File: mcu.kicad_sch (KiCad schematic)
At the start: 54 parts, among them J69 Conn_01x22, J70 Conn_01x22, J71 Conn_01x22, J72 Conn_01x22, J73 Conn_01x22, J74 Conn_01x22, J75 Conn_01x22, J76 Conn_01x22, J77 Conn_01x22, J78 Conn_01x22

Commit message: WIP v0.2.0 changes
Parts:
- removed J69, J70, J71, J72, J73, J74, J75, J76, J77, J78: Conn_01x22, HL_Connector_Pad_2.54mm:Pad_1x22_P2.54_1.7x1.7_Oct, symbol Connector_Generic:Conn_01x22
- removed R120, R121, R147, R148, R149, R150, R151, R152, R153, R154, R155, R156, R157, R158, R159: 1k, Resistor_SMD:R_0402_1005Metric, symbol Device:R_Small
- added J63, J64, J65, J66, J92, J93, J94, J95: Conn_01x20, HL_Connector_Pad_2.54mm:Pad_1x20_P2.54_1.7x1.7_Oct, symbol Connector_Generic:Conn_01x20
- added J96, J97: Conn_01x03, HL_Connector_Pad_2.54mm:Pad_1x03_P2.54_1.7x1.7_Rnd-Rect-Rnd, symbol Connector_Generic:Conn_01x03
- added U36: RPi_Pico_SMD_TH, HL_Module:RPi_Pico_Outline, symbol HL_MCU_Module:RPi_Pico_SMD_TH
- R129, R130: value 1k -> 3.3k; footprint Resistor_SMD:R_0402_1005Metric -> Resistor_SMD:R_0603_1608Metric; LCSC C11702 -> C22978
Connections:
- net at R126.1: now also J63.7 (Pin_7)
- net at R126.2: now also J64.7 (Pin_7), J92.7 (Pin_7), J93.7 (Pin_7), U36.34 (GPIO28_ADC2)
- net at R146.1: now also J66.1 (Pin_1)
- net at R146.2: now also J65.1 (Pin_1), J94.1 (Pin_1), J95.1 (Pin_1), U36.1 (GPIO0)
- net at R138.1: now also J66.11 (Pin_11)
- net at R139.1: now also J66.10 (Pin_10)
- net at R140.1: now also J66.9 (Pin_9)
- net at R141.1: now also J66.7 (Pin_7)
- net at R142.1: now also J66.6 (Pin_6)
- net at R143.1: now also J66.5 (Pin_5)
- net at R144.1: now also J66.4 (Pin_4)
- net at R145.1: now also J66.2 (Pin_2)
- net at R116.2: now also J64.20 (Pin_20), J92.20 (Pin_20), J93.20 (Pin_20), U36.21 (GPIO16)
- net at R125.2: now also J64.9 (Pin_9), J92.9 (Pin_9), J93.9 (Pin_9), U36.32 (GPIO27_ADC1)
- net at R127.2: now also J64.6 (Pin_6), J92.6 (Pin_6), J93.6 (Pin_6), U36.35 (ADC_VREF)
- net +3.3V: now reaches R128.2
- net +3.3V: now also R129.1, R130.1, J64.5 (Pin_5), J92.5 (Pin_5), J93.5 (Pin_5), U36.36 (3V3)
- net SCL: now reaches R129.2
- net SCL: now also J63.14 (Pin_14), J64.14 (Pin_14), J92.14 (Pin_14), J93.14 (Pin_14), U36.27 (GPIO21)
- net SDA: now reaches R130.2
- net SDA: now also J63.15 (Pin_15), J64.15 (Pin_15), J92.15 (Pin_15), J93.15 (Pin_15), U36.26 (GPIO20)
- net at R131.2: now also J65.20 (Pin_20), J94.20 (Pin_20), J95.20 (Pin_20), U36.20 (GPIO15)
- net at R132.2: now also J65.19 (Pin_19), J94.19 (Pin_19), J95.19 (Pin_19), U36.19 (GPIO14)
- net at R133.2: now also J65.17 (Pin_17), J94.17 (Pin_17), J95.17 (Pin_17), U36.17 (GPIO13)
- net at R134.2: now also J65.16 (Pin_16), J94.16 (Pin_16), J95.16 (Pin_16), U36.16 (GPIO12)
- net at R117.2: now also J64.19 (Pin_19), J92.19 (Pin_19), J93.19 (Pin_19), U36.22 (GPIO17)
- net at R135.2: now also J65.15 (Pin_15), J94.15 (Pin_15), J95.15 (Pin_15), U36.15 (GPIO11)
- net at R136.2: now also J65.14 (Pin_14), J94.14 (Pin_14), J95.14 (Pin_14), U36.14 (GPIO10)
- net at R137.2: now also J65.12 (Pin_12), J94.12 (Pin_12), J95.12 (Pin_12), U36.12 (GPIO9)
- net at R118.2: now also J64.17 (Pin_17), J92.17 (Pin_17), J93.17 (Pin_17), U36.24 (GPIO18)
- net at R119.2: now also J64.16 (Pin_16), J92.16 (Pin_16), J93.16 (Pin_16), U36.25 (GPIO19)
- net at R122.2: now also J64.12 (Pin_12), J92.12 (Pin_12), J93.12 (Pin_12), U36.29 (GPIO22)
- net at R123.2: now also J64.11 (Pin_11), J92.11 (Pin_11), J93.11 (Pin_11), U36.30 (RUN)
- net at R124.2: now also J64.10 (Pin_10), J92.10 (Pin_10), J93.10 (Pin_10), U36.31 (GPIO26_ADC0)
- net at R138.2: now also J65.11 (Pin_11), J94.11 (Pin_11), J95.11 (Pin_11), U36.11 (GPIO8)
- net at R139.2: now also J65.10 (Pin_10), J94.10 (Pin_10), J95.10 (Pin_10), U36.10 (GPIO7)
- net at R140.2: now also J65.9 (Pin_9), J94.9 (Pin_9), J95.9 (Pin_9), U36.9 (GPIO6)
- net at R141.2: now also J65.7 (Pin_7), J94.7 (Pin_7), J95.7 (Pin_7), U36.7 (GPIO5)
- net at R142.2: now also J65.6 (Pin_6), J94.6 (Pin_6), J95.6 (Pin_6), U36.6 (GPIO4)
- net at R143.2: now also J65.5 (Pin_5), J94.5 (Pin_5), J95.5 (Pin_5), U36.5 (GPIO3)
- net at R144.2: now also J65.4 (Pin_4), J94.4 (Pin_4), J95.4 (Pin_4), U36.4 (GPIO2)
- net at R145.2: now also J65.2 (Pin_2), J94.2 (Pin_2), J95.2 (Pin_2), U36.2 (GPIO1)
- net at R133.1: now also J66.17 (Pin_17)
- net at R137.1: now also J66.12 (Pin_12)
- net at R134.1: now also J66.16 (Pin_16)
- net at R116.1: now also J63.20 (Pin_20)
- net at R135.1: now also J66.15 (Pin_15)
- net at R128.1: now also J63.5 (Pin_5)
- net at R125.1: now also J63.9 (Pin_9)
- net at R127.1: now also J63.6 (Pin_6)
- net at R131.1: now also J66.20 (Pin_20)
- net at R132.1: now also J66.19 (Pin_19)
- net at R117.1: now also J63.19 (Pin_19)
- net at R136.1: now also J66.14 (Pin_14)
- net at R118.1: now also J63.17 (Pin_17)
- net at R119.1: now also J63.16 (Pin_16)
- net at R122.1: now also J63.12 (Pin_12)
- net at R123.1: now also J63.11 (Pin_11)
- net at R124.1: now also J63.10 (Pin_10)
- new net: J63.2 (Pin_2), J64.2 (Pin_2), J92.2 (Pin_2), J93.2 (Pin_2), U36.39 (VSYS)
- new net: J63.4 (Pin_4), J64.4 (Pin_4), J92.4 (Pin_4), J93.4 (Pin_4), U36.37 (3V3_EN)
- new net: J63.8 (Pin_8), J64.8 (Pin_8), J92.8 (Pin_8), J93.8 (Pin_8), U36.33 (AGND)
- new net: J96.1 (Pin_1), J97.1 (Pin_1), U36.43 (SWDIO)
- new net: J96.3 (Pin_3), J97.3 (Pin_3), U36.41 (SWCLK)
- new net +5V: J63.1 (Pin_1), J64.1 (Pin_1), J92.1 (Pin_1), J93.1 (Pin_1), U36.40 (VBUS)
- new net GND: J63.13 (Pin_13), J63.18 (Pin_18), J63.3 (Pin_3), J64.13 (Pin_13), J64.18 (Pin_18), J64.3 (Pin_3), J65.13 (Pin_13), J65.18 (Pin_18), J65.3 (Pin_3), J65.8 (Pin_8), J66.13 (Pin_13), J66.18 (Pin_18), J66.3 (Pin_3), J66.8 (Pin_8), J92.13 (Pin_13), J92.18 (Pin_18), J92.3 (Pin_3), J93.13 (Pin_13), J93.18 (Pin_18), J93.3 (Pin_3), J94.13 (Pin_13), J94.18 (Pin_18), J94.3 (Pin_3), J94.8 (Pin_8), J95.13 (Pin_13), J95.18 (Pin_18), J95.3 (Pin_3), J95.8 (Pin_8), J96.2 (Pin_2), J97.2 (Pin_2), U36.13 (GND), U36.18 (GND), U36.23 (GND), U36.28 (GND), U36.3 (GND), U36.38 (GND), U36.42 (GND), U36.8 (GND)

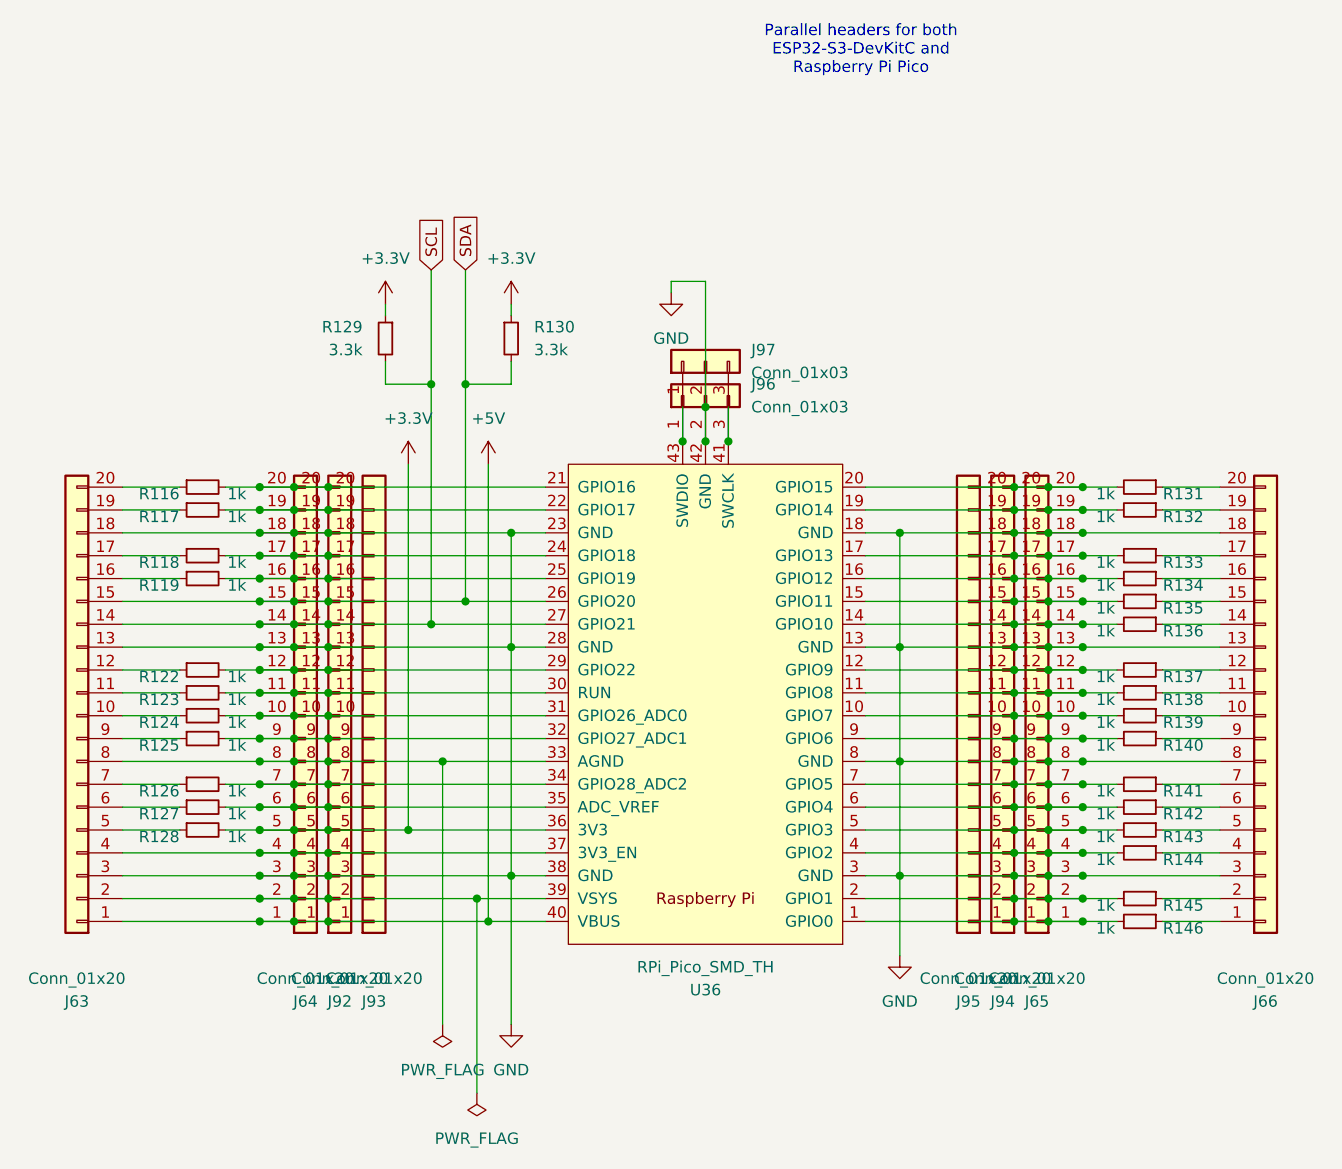
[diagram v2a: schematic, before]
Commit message: Assign part numbers and finish other 0.2.0 changes
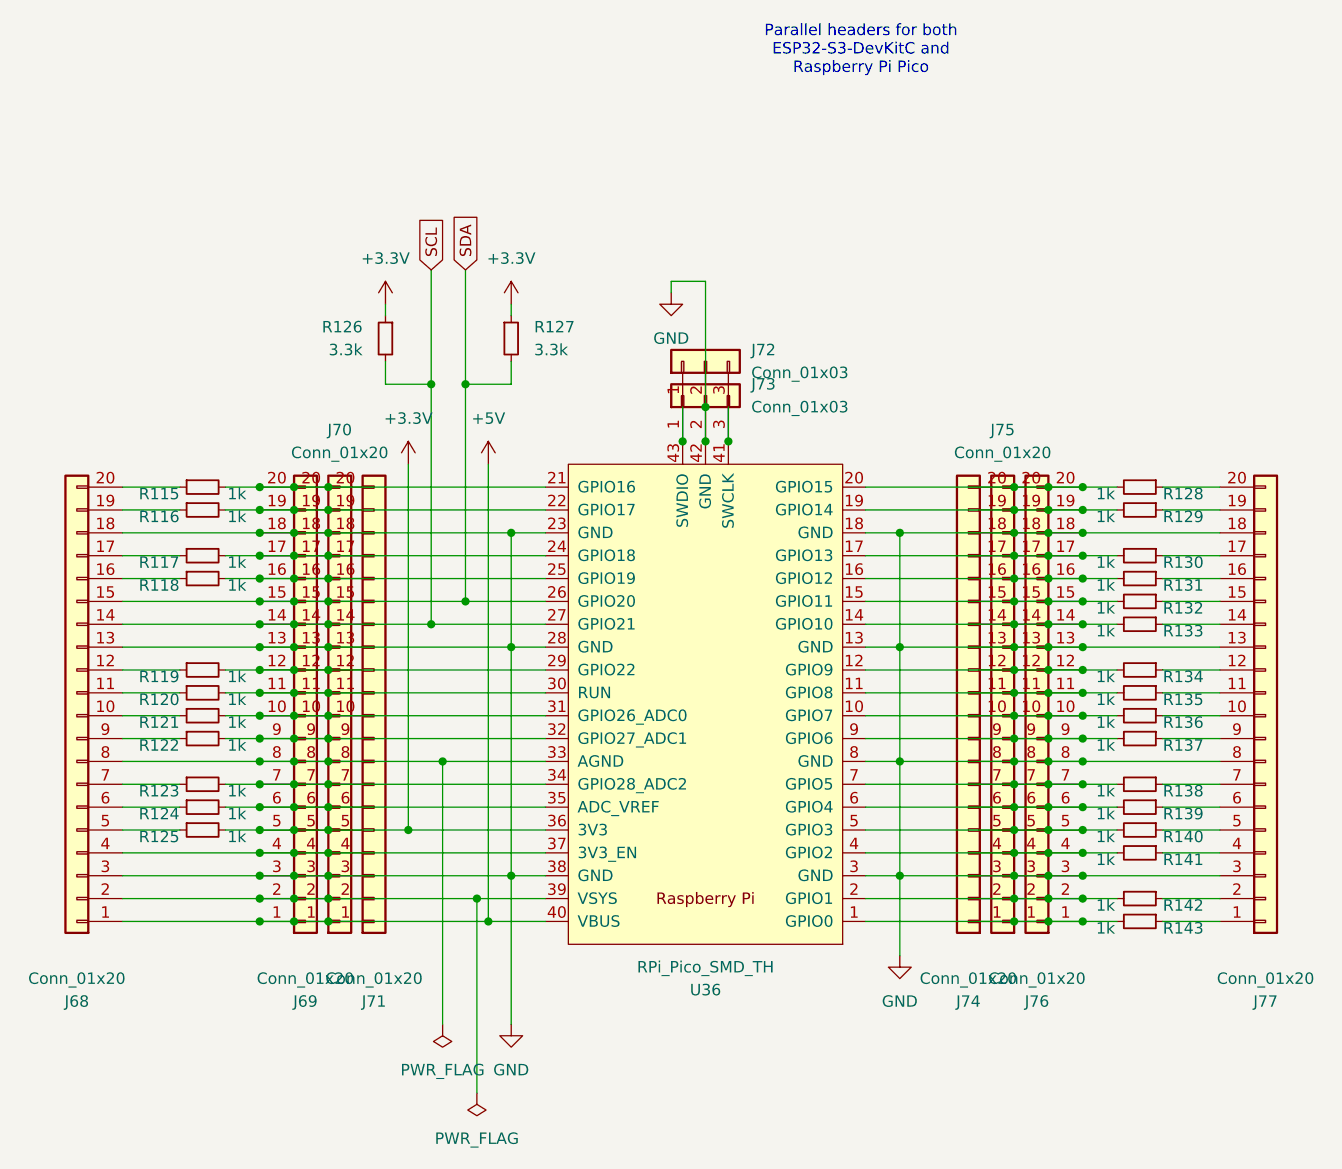
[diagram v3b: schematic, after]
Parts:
- J68: renamed from J63; LCSC (none) -> C50981
- J69: renamed from J64; LCSC§ (none) -> C50981
- J70: renamed from J92; LCSC (none) -> C2905423
- J75: renamed from J94; LCSC (none) -> C2905423
- J76: renamed from J65; LCSC (none) -> C50981
- J77: renamed from J66; LCSC (none) -> C50981
- renumbered J93 to J71, J97 to J72, J96 to J73, J95 to J74, R116 to R115, R117 to R116, R118 to R117, R119 to R118, R122 to R119, R123 to R120, R124 to R121, R125 to R122, R126 to R123, R127 to R124, R128 to R125, R129 to R126, R130 to R127, R131 to R128, R132 to R129, R133 to R130, R134 to R131, R135 to R132, R136 to R133, R137 to R134, R138 to R135, R139 to R136, R140 to R137, R141 to R138, R142 to R139, R143 to R140, R144 to R141, R145 to R142, R146 to R143

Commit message: Update the title blocks
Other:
- company: (none) -> Hat Labs Oy
- title: (none) -> HALSPA - Hat Labs Spaghetti Board
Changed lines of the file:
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@@
 	(generator_version "9.0")
 	(paper "A4")
+	(title_block
+		(title "HALSPA - Hat Labs Spaghetti Board")
+		(date "2025-04-17")
+		(rev "v0.2.0")
+		(company "Hat Labs Oy")
+		(comment 1 "See the accompanying LICENSE.md file for license details.")
+	)
 	(text "Parallel headers for both\nESP32-S3-DevKitC and\nRaspberry Pi Pico"
 		(exclude_from_sim no)

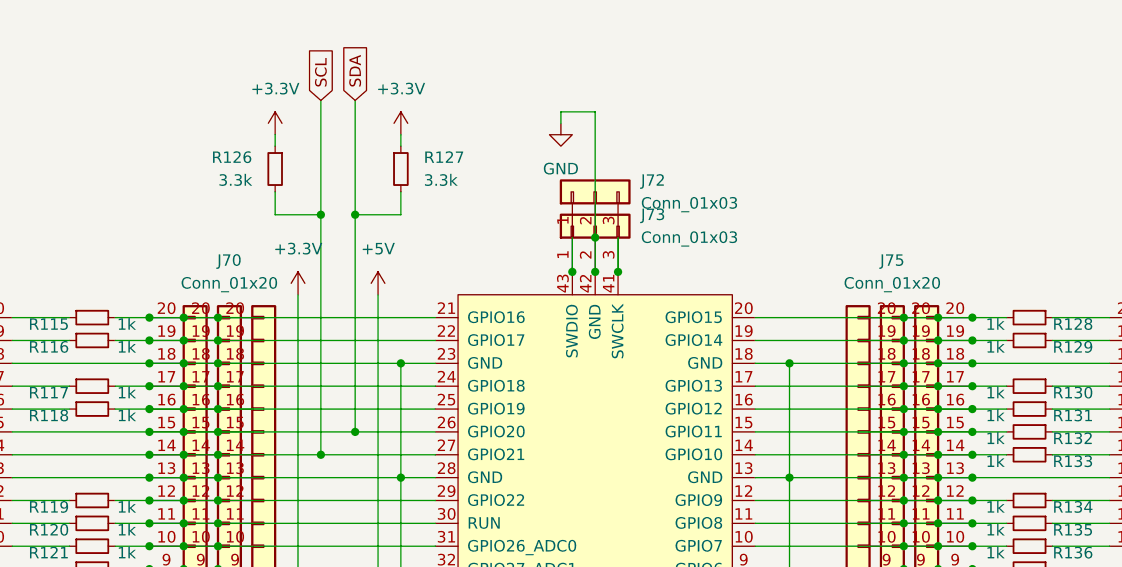
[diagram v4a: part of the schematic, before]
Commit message: Add JLCPCB corrections
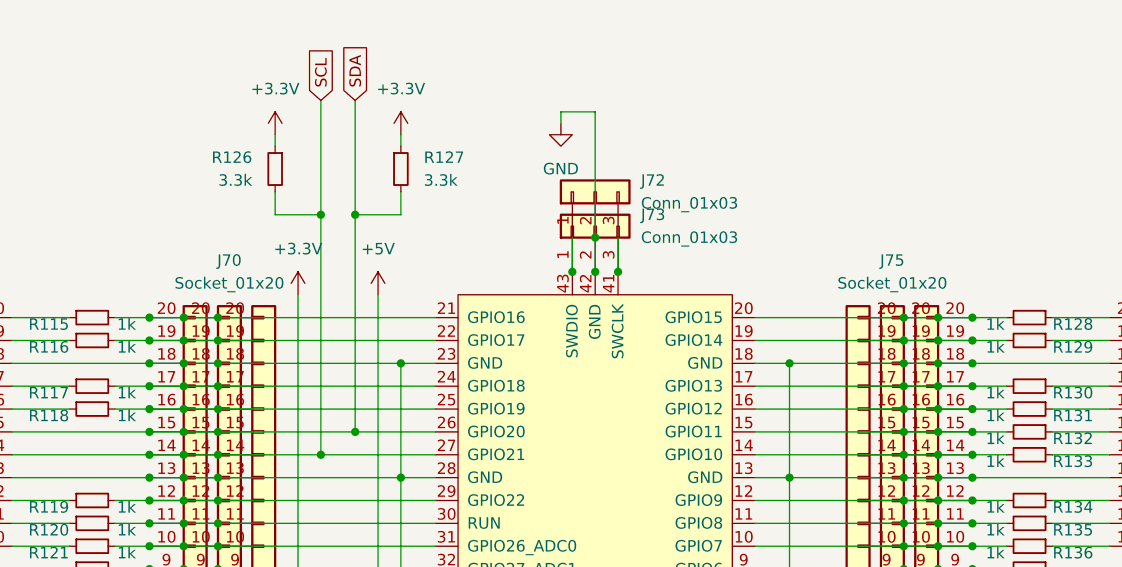
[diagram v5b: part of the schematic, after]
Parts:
- J68, J76, J77: JLCPCB_CORRECTION (none) -> 0;24.13;270
- J69: JLCPCB_CORRECTION (none) -> 0;24.13;270; LCSC (none) -> C50981; LCSC§ C50981 -> (none)
- J70, J75: value Conn_01x20 -> Socket_01x20; JLCPCB_CORRECTION (none) -> 0;24.13;270
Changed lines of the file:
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@@
+			)
+		)
+		(property "JLCPCB_CORRECTION" "0;24.13;270"
+			(at 171.45 96.52 0)
+			(effects
+				(font
+					(size 1.27 1.27)
+				)
+				(hide yes)
 			)
 		)
@@
 			)
 		)
-		(property "Value" "Conn_01x20"
+		(property "Value" "Socket_01x20"
 			(at 93.98 67.31 0)
 			(effects
@@
 		)
 		(property "LCSC" "C2905423"
+			(at 93.98 96.52 0)
+			(effects
+				(font
+					(size 1.27 1.27)
+				)
+				(hide yes)
+			)
+		)
+		(property "JLCPCB_CORRECTION" "0;24.13;270"
 			(at 93.98 96.52 0)
 			(effects
@@
 			)
 		)
-		(property "LCSC§" "C50981"
+		(property "LCSC" "C50981"
+			(at 90.17 96.52 0)
+			(effects
+				(font
+					(size 1.27 1.27)
+				)
+				(hide yes)
+			)
+		)
+		(property "JLCPCB_CORRECTION" "0;24.13;270"
 			(at 90.17 96.52 0)
 			(effects
@@
 			)
 		)
-		(property "Value" "Conn_01x20"
+		(property "Value" "Socket_01x20"
 			(at 167.64 67.31 0)
 			(effects
@@
 		)
 		(property "LCSC" "C2905423"
+			(at 167.64 96.52 0)
+			(effects
+				(font
+					(size 1.27 1.27)
+				)
+				(hide yes)
+			)
+		)
+		(property "JLCPCB_CORRECTION" "0;24.13;270"
 			(at 167.64 96.52 0)
 			(effects
@@
 			)
 		)
+		(property "JLCPCB_CORRECTION" "0;24.13;270"
+			(at 196.85 96.52 0)
+			(effects
+				(font
+					(size 1.27 1.27)
+				)
+				(hide yes)
+			)
+		)
 		(pin "2"
 		)
@@
 			(at 64.77 96.52 0)
 			(effects
+				(font
+					(size 1.27 1.27)
+				)
+				(hide yes)
+			)
+		)
+		(property "JLCPCB_CORRECTION" "0;24.13;270"
+			(at 64.77 96.52 0)
+			(effects

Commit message: Improve MCU2 layout; document curlim12v CSA
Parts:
- renumbered R115 to R116, R116 to R117, R117 to R118, R118 to R119, R119 to R120, R120 to R121, R121 to R122, R122 to R123, R123 to R124, R124 to R125, R125 to R126, R126 to R127, R127 to R128, R128 to R129, R129 to R130, R130 to R131, R131 to R132, R132 to R133, R133 to R134, R134 to R135, R135 to R136, R136 to R137, R137 to R138, R138 to R139, R139 to R140, R140 to R141, R141 to R142, R142 to R143, R143 to R144
